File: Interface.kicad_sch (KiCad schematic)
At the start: 44 parts, among them J5901 HEATER, J5902 HEATER, J5903 HEATER, J5904 HEATER, J6101 PV, J6102 PV, J6103 VBUS, J6104 PV, J6105 PV, J6106 PV, J6107 PV, J6108 Chan, J6109 Chan, J6110 Chan, J6111 Chan, J6112 Chan, J6113 Chan, J6114 HEADER_PV, J6115 HEADER_PV, J6116 HEADER_CHAN, J6117 HEADER_CHAN, J6118 HEADER_CHAN, J6119 HEADER_CHAN, J6120 Chan_BUS, J6121 Chan_BUS, J6122 VBUS, J6123 Chan, J6124 Chan, J6125 BATT_PACK, J6126 BATT_PACK, J6127 SPI, J6128 UART, J6129 VBUS, J6130 VBUS, J6131 Battery, J6132 Battery

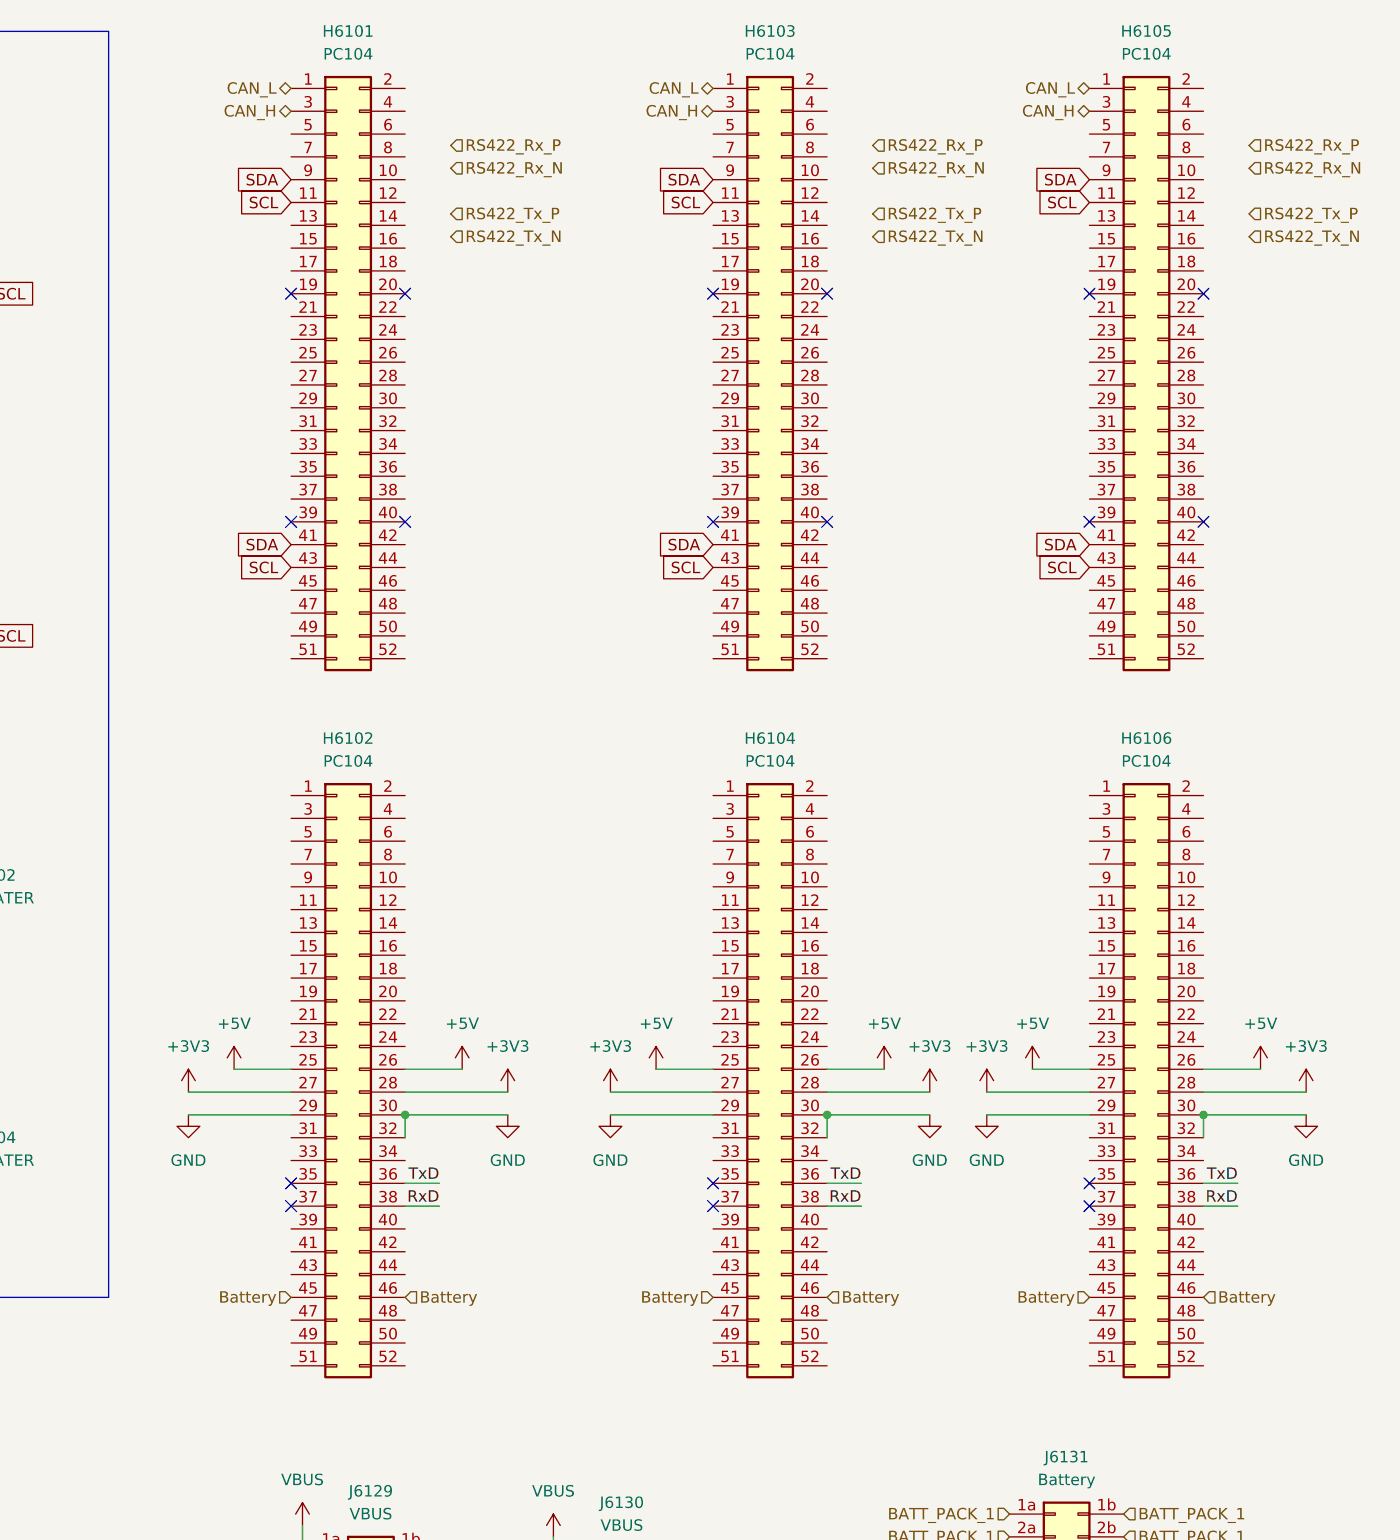
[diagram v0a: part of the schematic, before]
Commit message: deleted switch conncected to both batteries, modev pc104 connector to ti own sheet
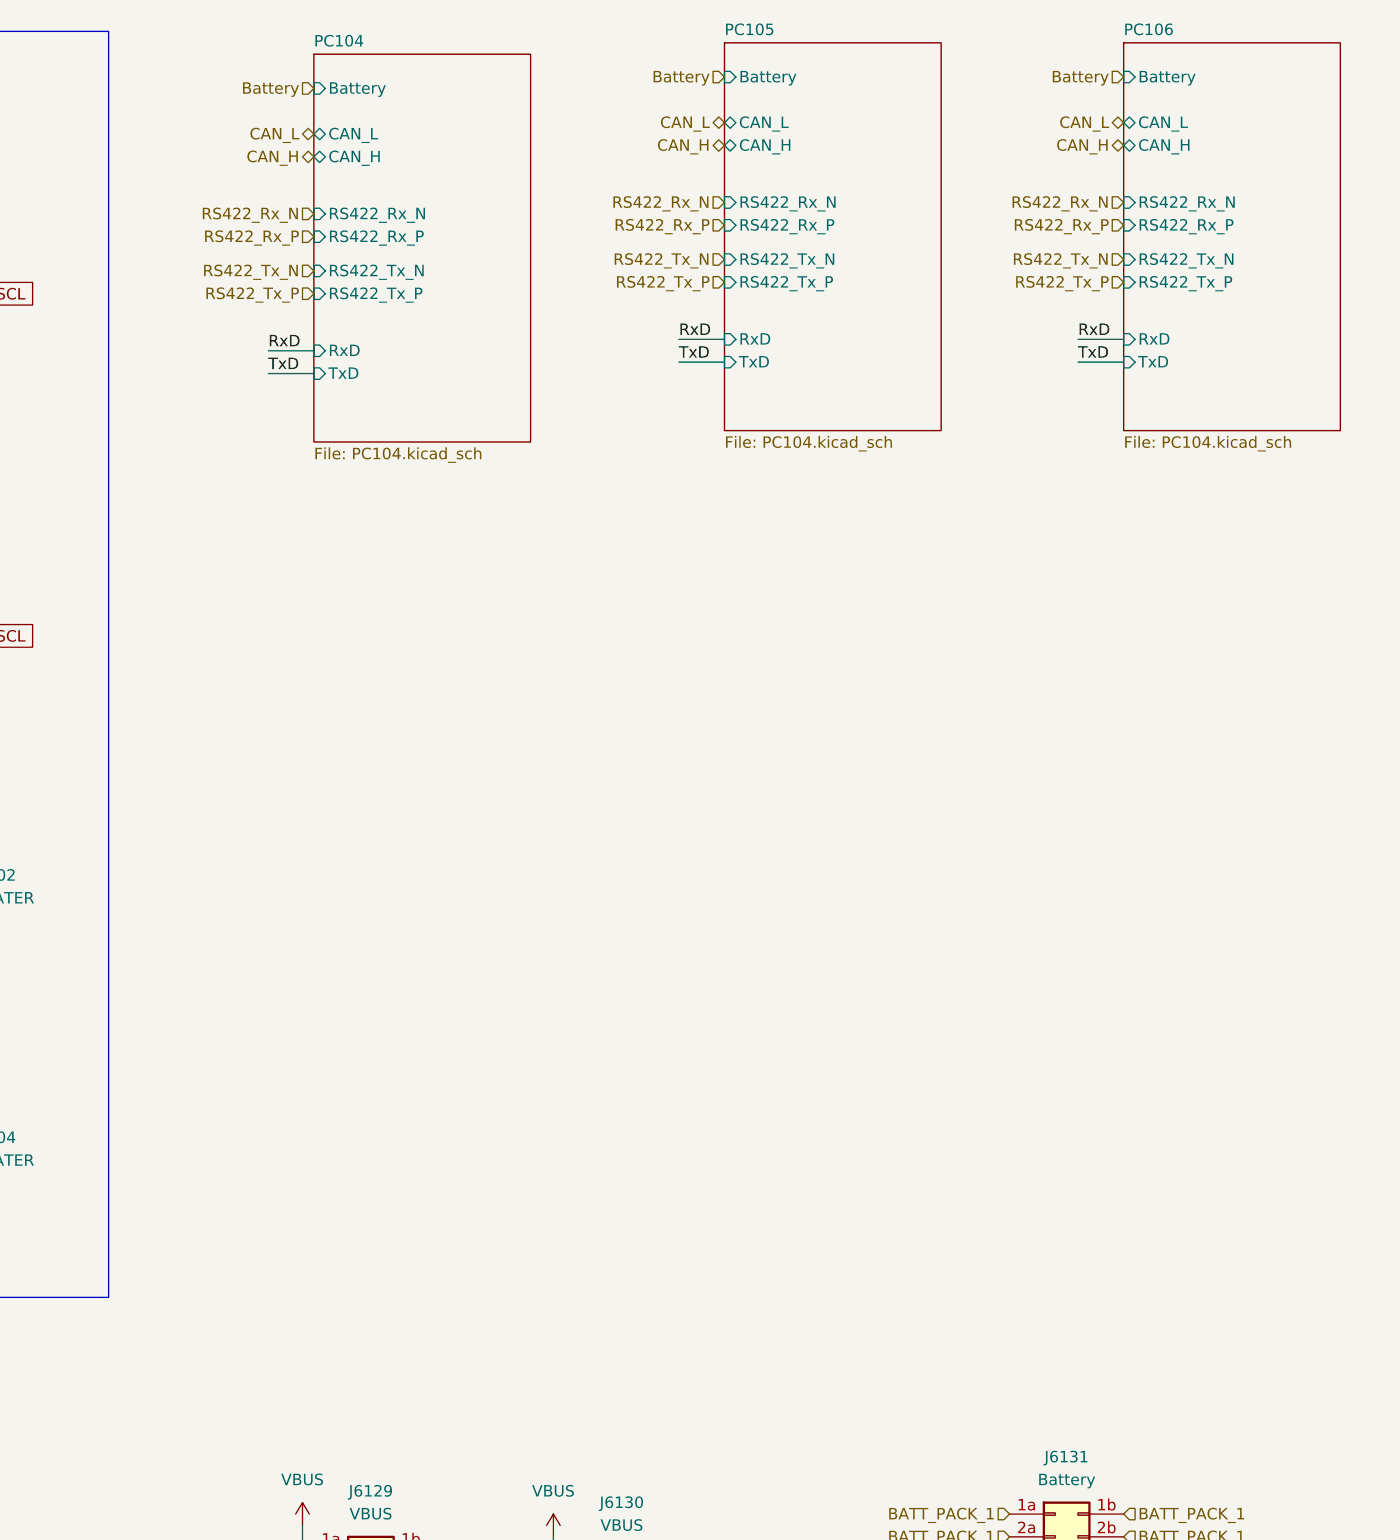
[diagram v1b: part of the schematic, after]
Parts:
- removed H6101, H6102, H6103, H6104, H6105, H6106: PC104, Connector_PinSocket_2.54mm:PinSocket_2x26_P2.54mm_Vertical, symbol Connector_Generic:Conn_02x26_Odd_Even
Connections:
- no-connect marks 18 -> 0
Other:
- added sheet PC104 (PC104.kicad_sch)
- added sheet PC105 (PC104.kicad_sch)
- added sheet PC106 (PC104.kicad_sch)

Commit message: replaced individual CC sourses for SOL with a single one
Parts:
- J6103, J6120, J6121, J6122, J6129, J6130: footprint (none) -> Connector_Harwin:Harwin_Gecko-G125-FVX1205L0X_2x06_P1.25mm_Vertical; symbol Connector_Generic:Conn_02x06_Row_Letter_Last -> Connector_Generic:Conn_02x06_Top_Bottom
- J6117: footprint (none) -> Connector_PinSocket_2.54mm:PinSocket_1x10_P2.54mm_Vertical
- J6131, J6132: footprint (none) -> Connector_Harwin:Harwin_Gecko-G125-FVX1605L0X_2x08_P1.25mm_Vertical; symbol Connector_Generic:Conn_02x08_Row_Letter_Last -> Connector_Generic:Conn_02x08_Top_Bottom
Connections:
- net BATT_PACK_1: now also J6131.1 (Pin_1), J6131.10 (Pin_10), J6131.2 (Pin_2), J6131.9 (Pin_9); no longer J6131.1a (Pin_1a), J6131.1b (Pin_1b), J6131.2a (Pin_2a), J6131.2b (Pin_2b)
- net BATT_PACK_2: now also J6132.1 (Pin_1), J6132.10 (Pin_10), J6132.2 (Pin_2), J6132.9 (Pin_9); no longer J6132.1a (Pin_1a), J6132.1b (Pin_1b), J6132.2a (Pin_2a), J6132.2b (Pin_2b)
- net Channel_10: now also J6121.1 (Pin_1), J6121.2 (Pin_2), J6121.3 (Pin_3), J6121.4 (Pin_4), J6121.5 (Pin_5), J6121.6 (Pin_6); no longer J6121.1a (Pin_1a), J6121.2a (Pin_2a), J6121.3a (Pin_3a), J6121.4a (Pin_4a), J6121.5a (Pin_5a), J6121.6a (Pin_6a)
- net Channel_9: now also J6120.1 (Pin_1), J6120.2 (Pin_2), J6120.3 (Pin_3), J6120.4 (Pin_4), J6120.5 (Pin_5), J6120.6 (Pin_6); no longer J6120.1a (Pin_1a), J6120.2a (Pin_2a), J6120.3a (Pin_3a), J6120.4a (Pin_4a), J6120.5a (Pin_5a), J6120.6a (Pin_6a)
- net GND: now also J6103.10 (Pin_10), J6103.11 (Pin_11), J6103.12 (Pin_12), J6103.7 (Pin_7), J6103.8 (Pin_8), J6103.9 (Pin_9), J6120.10 (Pin_10), J6120.11 (Pin_11), J6120.12 (Pin_12), J6120.7 (Pin_7), J6120.8 (Pin_8), J6120.9 (Pin_9), J6121.10 (Pin_10), J6121.11 (Pin_11), J6121.12 (Pin_12), J6121.7 (Pin_7), J6121.8 (Pin_8), J6121.9 (Pin_9), J6122.10 (Pin_10), J6122.11 (Pin_11), J6122.12 (Pin_12), J6122.7 (Pin_7), J6122.8 (Pin_8), J6122.9 (Pin_9), J6129.10 (Pin_10), J6129.11 (Pin_11), J6129.12 (Pin_12), J6129.7 (Pin_7), J6129.8 (Pin_8), J6129.9 (Pin_9), J6130.10 (Pin_10), J6130.11 (Pin_11), J6130.12 (Pin_12), J6130.7 (Pin_7), J6130.8 (Pin_8), J6130.9 (Pin_9), J6131.11 (Pin_11), J6131.12 (Pin_12), J6131.14 (Pin_14), J6131.3 (Pin_3), J6131.4 (Pin_4), J6131.6 (Pin_6), J6132.11 (Pin_11), J6132.12 (Pin_12), J6132.14 (Pin_14), J6132.3 (Pin_3), J6132.4 (Pin_4), J6132.6 (Pin_6); no longer J6103.1b (Pin_1b), J6103.2b (Pin_2b), J6103.3b (Pin_3b), J6103.4b (Pin_4b), J6103.5b (Pin_5b), J6103.6b (Pin_6b), J6120.1b (Pin_1b), J6120.2b (Pin_2b), J6120.3b (Pin_3b), J6120.4b (Pin_4b), J6120.5b (Pin_5b), J6120.6b (Pin_6b), J6121.1b (Pin_1b), J6121.2b (Pin_2b), J6121.3b (Pin_3b), J6121.4b (Pin_4b), J6121.5b (Pin_5b), J6121.6b (Pin_6b), J6122.1b (Pin_1b), J6122.2b (Pin_2b), J6122.3b (Pin_3b), J6122.4b (Pin_4b), J6122.5b (Pin_5b), J6122.6b (Pin_6b), J6129.1b (Pin_1b), J6129.2b (Pin_2b), J6129.3b (Pin_3b), J6129.4b (Pin_4b), J6129.5b (Pin_5b), J6129.6b (Pin_6b), J6130.1b (Pin_1b), J6130.2b (Pin_2b), J6130.3b (Pin_3b), J6130.4b (Pin_4b), J6130.5b (Pin_5b), J6130.6b (Pin_6b), J6131.3a (Pin_3a), J6131.3b (Pin_3b), J6131.4a (Pin_4a), J6131.4b (Pin_4b), J6131.6a (Pin_6a), J6131.6b (Pin_6b), J6132.3a (Pin_3a), J6132.3b (Pin_3b), J6132.4a (Pin_4a), J6132.4b (Pin_4b), J6132.6a (Pin_6a), J6132.6b (Pin_6b)
- net HEAT_BATT_1: now also J6131.16 (Pin_16), J6131.8 (Pin_8); no longer J6131.8a (Pin_8a), J6131.8b (Pin_8b)
- net HEAT_BATT_2: now also J6132.16 (Pin_16), J6132.8 (Pin_8); no longer J6132.8a (Pin_8a), J6132.8b (Pin_8b)
- net SCL: now also J6131.15 (Pin_15), J6132.15 (Pin_15); no longer J6131.7b (Pin_7b), J6132.7b (Pin_7b)
- net SDA: now also J6131.7 (Pin_7), J6132.7 (Pin_7); no longer J6131.7a (Pin_7a), J6132.7a (Pin_7a)
- net TMEAS_BATT_1: now also J6131.13 (Pin_13), J6131.5 (Pin_5); no longer J6131.5a (Pin_5a), J6131.5b (Pin_5b)
- net TMEAS_BATT_2: now also J6132.13 (Pin_13), J6132.5 (Pin_5); no longer J6132.5a (Pin_5a), J6132.5b (Pin_5b)
- net VBUS: now also J6103.1 (Pin_1), J6103.2 (Pin_2), J6103.3 (Pin_3), J6103.4 (Pin_4), J6103.5 (Pin_5), J6103.6 (Pin_6), J6122.1 (Pin_1), J6122.2 (Pin_2), J6122.3 (Pin_3), J6122.4 (Pin_4), J6122.5 (Pin_5), J6122.6 (Pin_6), J6129.1 (Pin_1), J6129.2 (Pin_2), J6129.3 (Pin_3), J6129.4 (Pin_4), J6129.5 (Pin_5), J6129.6 (Pin_6), J6130.1 (Pin_1), J6130.2 (Pin_2), J6130.3 (Pin_3), J6130.4 (Pin_4), J6130.5 (Pin_5), J6130.6 (Pin_6); no longer J6103.1a (Pin_1a), J6103.2a (Pin_2a), J6103.3a (Pin_3a), J6103.4a (Pin_4a), J6103.5a (Pin_5a), J6103.6a (Pin_6a), J6122.1a (Pin_1a), J6122.2a (Pin_2a), J6122.3a (Pin_3a), J6122.4a (Pin_4a), J6122.5a (Pin_5a), J6122.6a (Pin_6a), J6129.1a (Pin_1a), J6129.2a (Pin_2a), J6129.3a (Pin_3a), J6129.4a (Pin_4a), J6129.5a (Pin_5a), J6129.6a (Pin_6a), J6130.1a (Pin_1a), J6130.2a (Pin_2a), J6130.3a (Pin_3a), J6130.4a (Pin_4a), J6130.5a (Pin_5a), J6130.6a (Pin_6a)
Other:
- moved on the sheet: J6114, J6115, J6116, J6117, J6118, J6119, J6129

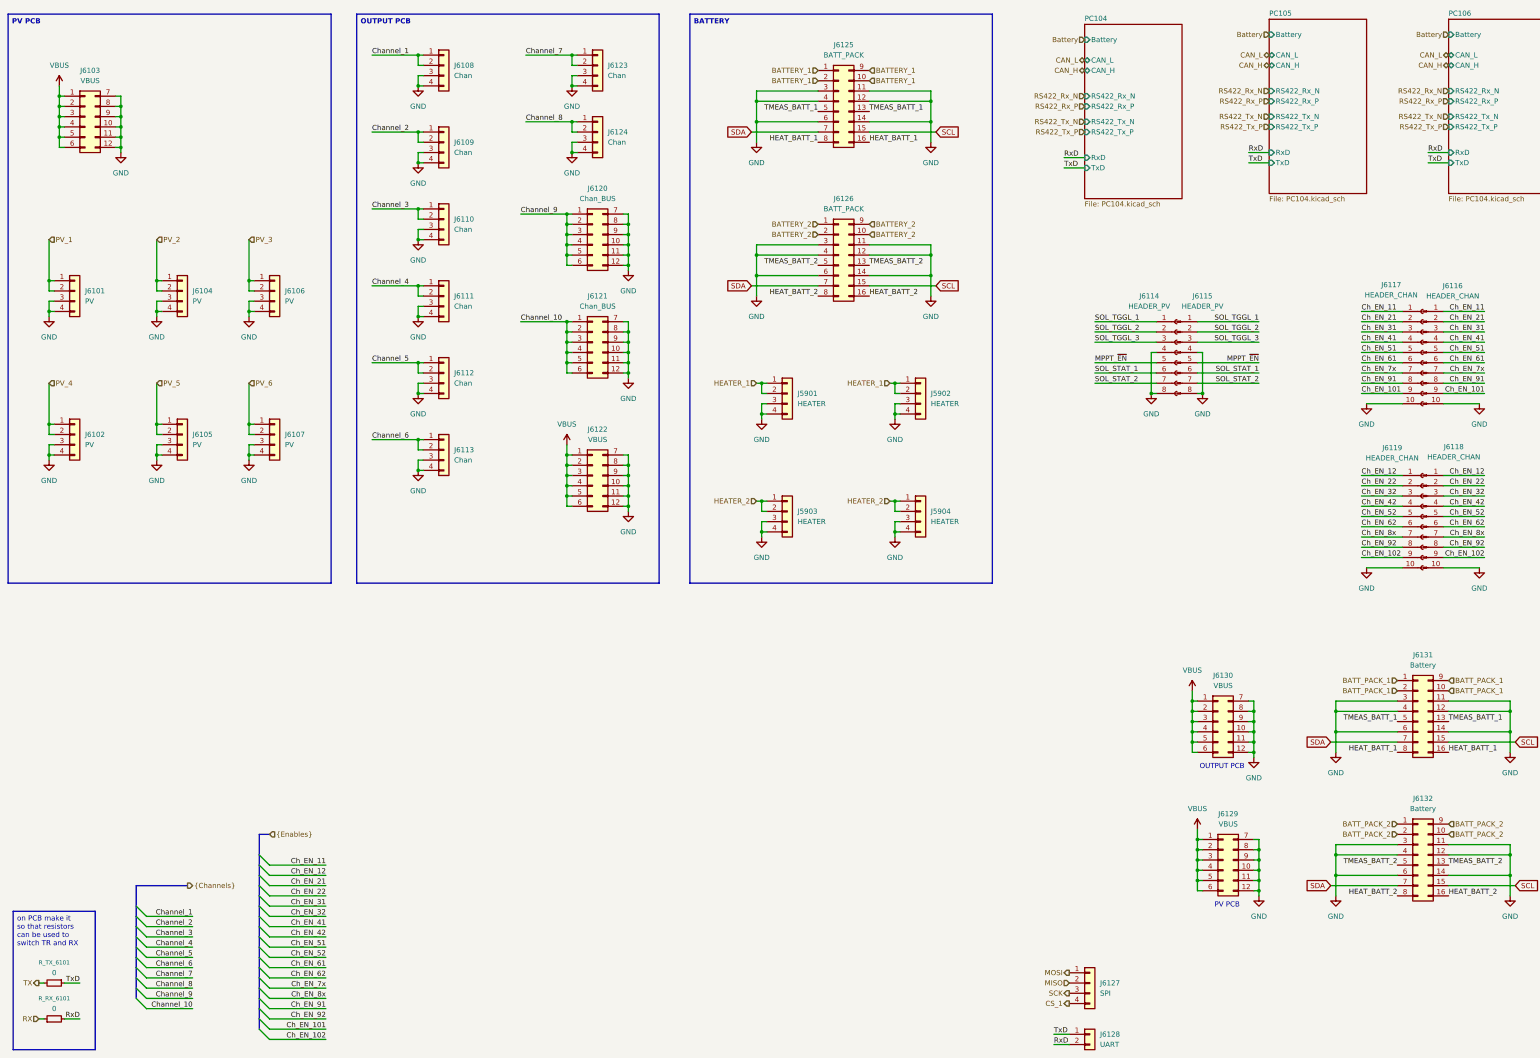
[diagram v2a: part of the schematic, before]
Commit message: restructurization of the entire project improved
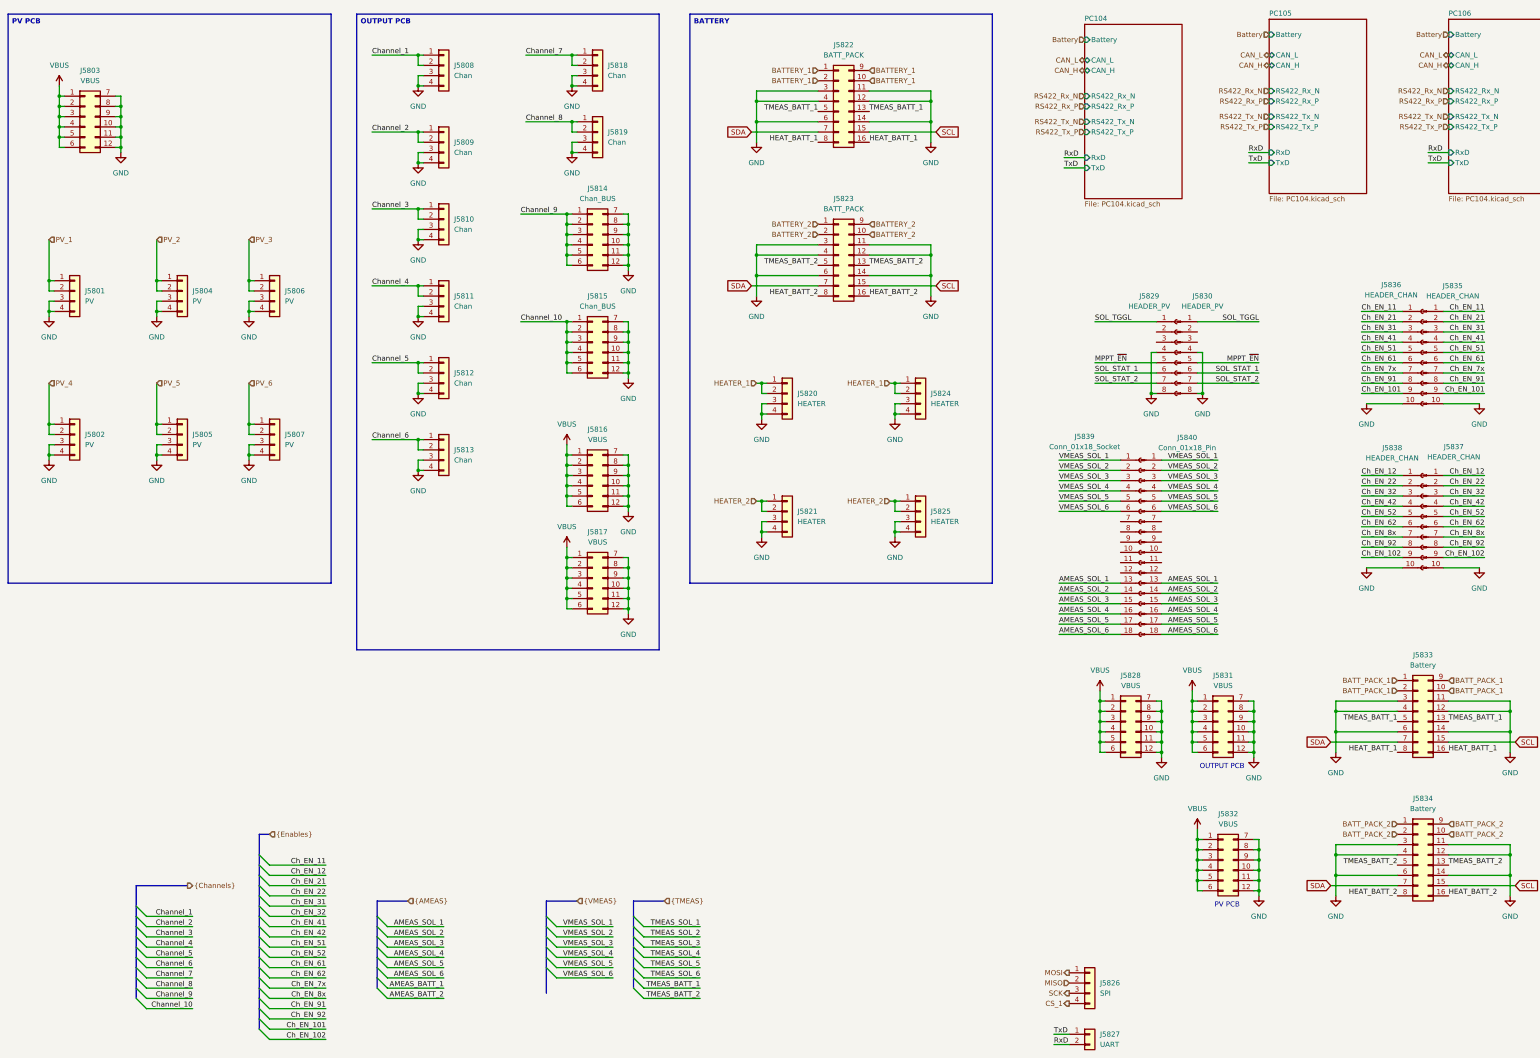
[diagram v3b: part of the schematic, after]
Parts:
- removed R_RX_6101, R_TX_6101: 0, Resistor_SMD:R_0603_1608Metric_Pad0.98x0.95mm_HandSolder, symbol Device:R_Small
- added J5817, J5828: VBUS, Connector_Harwin:Harwin_Gecko-G125-FVX1205L0X_2x06_P1.25mm_Vertical, symbol Connector_Generic:Conn_02x06_Top_Bottom
- added J5839: Conn_01x18_Socket, symbol Connector:Conn_01x18_Socket
- added J5840: Conn_01x18_Pin, symbol Connector:Conn_01x18_Pin
- J5808: renamed from J6108; footprint (none) -> Connector_Molex:Molex_CLIK-Mate_502494-0470_1x04-1MP_P2.00mm_Horizontal
- renumbered J6101 to J5801, J6102 to J5802, J6103 to J5803, J6104 to J5804, J6105 to J5805, J6106 to J5806, J6107 to J5807, J6109 to J5809, J6110 to J5810, J6111 to J5811, J6112 to J5812, J6113 to J5813, J6120 to J5814, J6121 to J5815, J6122 to J5816, J6123 to J5818, J6124 to J5819, J5901 to J5820, J5903 to J5821, J6125 to J5822, J6126 to J5823, J5902 to J5824, J5904 to J5825, J6127 to J5826, J6128 to J5827, J6114 to J5829, J6115 to J5830, J6130 to J5831, J6129 to J5832, J6131 to J5833, J6132 to J5834, J6116 to J5835, J6117 to J5836, J6118 to J5837, J6119 to J5838
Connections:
- net GND: now also J5817.10 (Pin_10), J5817.11 (Pin_11), J5817.12 (Pin_12), J5817.7 (Pin_7), J5817.8 (Pin_8), J5817.9 (Pin_9), J5828.10 (Pin_10), J5828.11 (Pin_11), J5828.12 (Pin_12), J5828.7 (Pin_7), J5828.8 (Pin_8), J5828.9 (Pin_9)
- net VBUS: now also J5817.1 (Pin_1), J5817.2 (Pin_2), J5817.3 (Pin_3), J5817.4 (Pin_4), J5817.5 (Pin_5), J5817.6 (Pin_6), J5828.1 (Pin_1), J5828.2 (Pin_2), J5828.3 (Pin_3), J5828.4 (Pin_4), J5828.5 (Pin_5), J5828.6 (Pin_6)
- net SOL_TGGL_1 renamed SOL_TGGL
- net SOL_TGGL_2: no longer names the net of J5829.2 (Pin_2)
- net SOL_TGGL_2: no longer J5830.2 (Pin_2)
- net SOL_TGGL_3: no longer names the net of J5829.3 (Pin_3)
- net SOL_TGGL_3: no longer J5830.3 (Pin_3)
- new net AMEAS_SOL_1: J5839.13 (Pin_13), J5840.13 (Pin_13)
- new net AMEAS_SOL_2: J5839.14 (Pin_14), J5840.14 (Pin_14)
- new net AMEAS_SOL_3: J5839.15 (Pin_15), J5840.15 (Pin_15)
- new net AMEAS_SOL_4: J5839.16 (Pin_16), J5840.16 (Pin_16)
- new net AMEAS_SOL_5: J5839.17 (Pin_17), J5840.17 (Pin_17)
- new net AMEAS_SOL_6: J5839.18 (Pin_18), J5840.18 (Pin_18)
- new net VMEAS_SOL_1: J5839.1 (Pin_1), J5840.1 (Pin_1)
- new net VMEAS_SOL_2: J5839.2 (Pin_2), J5840.2 (Pin_2)
- new net VMEAS_SOL_3: J5839.3 (Pin_3), J5840.3 (Pin_3)
- new net VMEAS_SOL_4: J5839.4 (Pin_4), J5840.4 (Pin_4)
- new net VMEAS_SOL_5: J5839.5 (Pin_5), J5840.5 (Pin_5)
- new net VMEAS_SOL_6: J5839.6 (Pin_6), J5840.6 (Pin_6)
